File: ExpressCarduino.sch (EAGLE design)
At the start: 14 parts, among them IC1 MCP23017ML, U1 AP3012

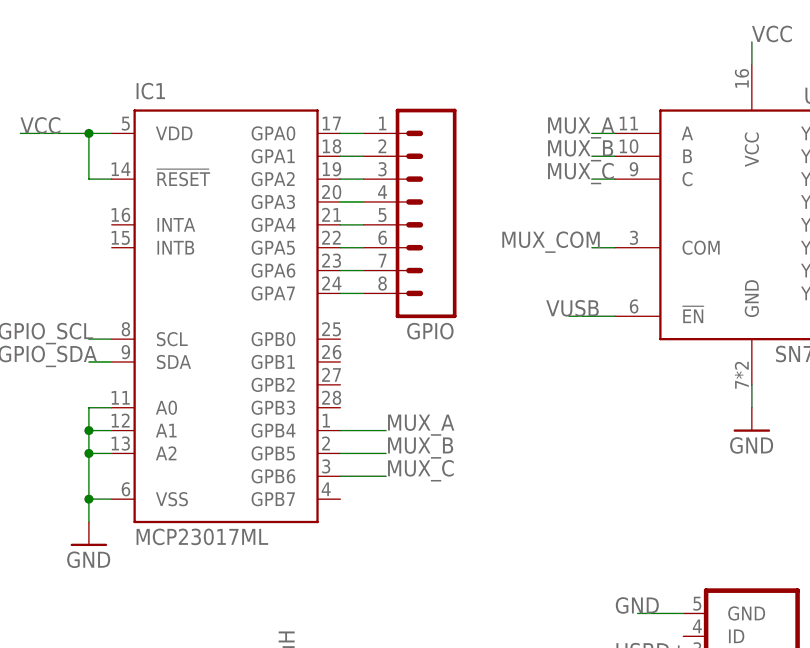
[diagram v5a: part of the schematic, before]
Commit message: Fixed pins for the mux and rearranged the board for better routing
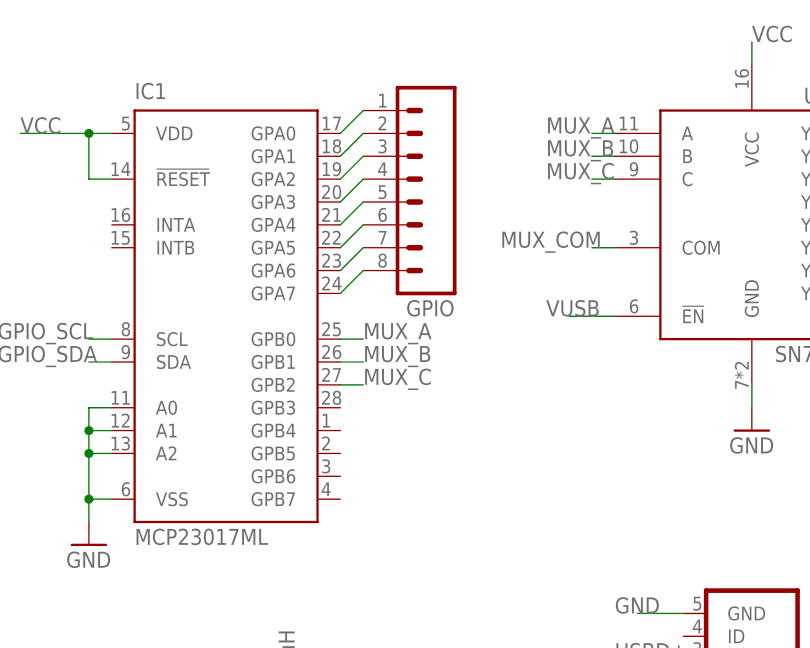
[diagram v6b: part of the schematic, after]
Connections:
- net MUX_A: now also IC1.GPB0; no longer IC1.GPB4
- net MUX_B: now also IC1.GPB1; no longer IC1.GPB5
- net MUX_C: now also IC1.GPB2; no longer IC1.GPB6
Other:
- moved on the sheet: GPIO
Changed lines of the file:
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@@
 <instance part="GND4" gate="1" x="53.34" y="63.5"/>
 <instance part="GND5" gate="1" x="127" y="76.2"/>
-<instance part="GPIO" gate="G$1" x="88.9" y="101.6" rot="R180"/>
+<instance part="GPIO" gate="G$1" x="88.9" y="104.14" rot="R180"/>
 <instance part="U$2" gate="G$1" x="127" y="99.06"/>
 <instance part="ADC" gate="G$1" x="147.32" y="101.6" rot="R180"/>
@@
 <segment>
 <pinref part="GPIO" gate="G$1" pin="1"/>
-<wire x1="83.82" y1="109.22" x2="81.28" y2="109.22" width="0.1524" layer="91"/>
+<wire x1="83.82" y1="111.76" x2="81.28" y2="109.22" width="0.1524" layer="91"/>
 <pinref part="IC1" gate="G$1" pin="GPA0"/>
 </segment>
@@
 <segment>
 <pinref part="GPIO" gate="G$1" pin="2"/>
-<wire x1="83.82" y1="106.68" x2="81.28" y2="106.68" width="0.1524" layer="91"/>
+<wire x1="83.82" y1="109.22" x2="81.28" y2="106.68" width="0.1524" layer="91"/>
 <pinref part="IC1" gate="G$1" pin="GPA1"/>
 </segment>
@@
 <segment>
 <pinref part="GPIO" gate="G$1" pin="3"/>
-<wire x1="83.82" y1="104.14" x2="81.28" y2="104.14" width="0.1524" layer="91"/>
+<wire x1="83.82" y1="106.68" x2="81.28" y2="104.14" width="0.1524" layer="91"/>
 <pinref part="IC1" gate="G$1" pin="GPA2"/>
 </segment>
@@
 <segment>
 <pinref part="GPIO" gate="G$1" pin="4"/>
-<wire x1="83.82" y1="101.6" x2="81.28" y2="101.6" width="0.1524" layer="91"/>
+<wire x1="83.82" y1="104.14" x2="81.28" y2="101.6" width="0.1524" layer="91"/>
 <pinref part="IC1" gate="G$1" pin="GPA3"/>
 </segment>
@@
 <segment>
 <pinref part="GPIO" gate="G$1" pin="5"/>
-<wire x1="83.82" y1="99.06" x2="81.28" y2="99.06" width="0.1524" layer="91"/>
+<wire x1="83.82" y1="101.6" x2="81.28" y2="99.06" width="0.1524" layer="91"/>
 <pinref part="IC1" gate="G$1" pin="GPA4"/>
 </segment>
@@
 <segment>
 <pinref part="GPIO" gate="G$1" pin="6"/>
-<wire x1="83.82" y1="96.52" x2="81.28" y2="96.52" width="0.1524" layer="91"/>
+<wire x1="83.82" y1="99.06" x2="81.28" y2="96.52" width="0.1524" layer="91"/>
 <pinref part="IC1" gate="G$1" pin="GPA5"/>
 </segment>
@@
 <segment>
 <pinref part="GPIO" gate="G$1" pin="7"/>
-<wire x1="83.82" y1="93.98" x2="81.28" y2="93.98" width="0.1524" layer="91"/>
+<wire x1="83.82" y1="96.52" x2="81.28" y2="93.98" width="0.1524" layer="91"/>
 <pinref part="IC1" gate="G$1" pin="GPA6"/>
 </segment>
@@
 <segment>
 <pinref part="GPIO" gate="G$1" pin="8"/>
-<wire x1="83.82" y1="91.44" x2="81.28" y2="91.44" width="0.1524" layer="91"/>
+<wire x1="83.82" y1="93.98" x2="81.28" y2="91.44" width="0.1524" layer="91"/>
 <pinref part="IC1" gate="G$1" pin="GPA7"/>
 </segment>
@@
 </segment>
 <segment>
-<pinref part="IC1" gate="G$1" pin="GPB4"/>
-<wire x1="81.28" y1="76.2" x2="86.36" y2="76.2" width="0.1524" layer="91"/>
-<label x="86.36" y="76.2" size="1.778" layer="95"/>
+<pinref part="IC1" gate="G$1" pin="GPB0"/>
+<wire x1="81.28" y1="86.36" x2="83.82" y2="86.36" width="0.1524" layer="91"/>
+<label x="83.82" y="86.36" size="1.778" layer="95"/>
 </segment>
 </net>
 <net name="MUX_B" class="0">
-<segment>
-<pinref part="IC1" gate="G$1" pin="GPB5"/>
-<wire x1="81.28" y1="73.66" x2="86.36" y2="73.66" width="0.1524" layer="91"/>
-<label x="86.36" y="73.66" size="1.778" layer="95"/>
-</segment>
 <segment>
 <pinref part="U$2" gate="G$1" pin="B"/>
@@
 <label x="104.14" y="106.68" size="1.778" layer="95"/>
 </segment>
+<segment>
+<pinref part="IC1" gate="G$1" pin="GPB1"/>
+<wire x1="81.28" y1="83.82" x2="83.82" y2="83.82" width="0.1524" layer="91"/>
+<label x="83.82" y="83.82" size="1.778" layer="95"/>
+</segment>
 </net>
 <net name="MUX_C" class="0">
-<segment>
-<pinref part="IC1" gate="G$1" pin="GPB6"/>
-<wire x1="81.28" y1="71.12" x2="86.36" y2="71.12" width="0.1524" layer="91"/>
-<label x="86.36" y="71.12" size="1.778" layer="95"/>
-</segment>
 <segment>
 <pinref part="U$2" gate="G$1" pin="C"/>
@@
 <label x="104.14" y="104.14" size="1.778" layer="95"/>
 </segment>
-</net>
+<segment>
+<pinref part="IC1" gate="G$1" pin="GPB2"/>
+<wire x1="81.28" y1="81.28" x2="83.82" y2="81.28" width="0.1524" layer="91"/>
+<label x="83.82" y="81.28" size="1.778" layer="95"/>
+</segment>
+</net>
